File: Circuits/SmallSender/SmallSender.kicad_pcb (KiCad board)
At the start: 2 copper layers, 28 x 49.6 mm, 13 parts, among them P1 WRITER-VCC, SW1 JB-15FBP2, SW2 MKA-10110, U1 TWE_LITE_SMD, U2 HN2S01FU

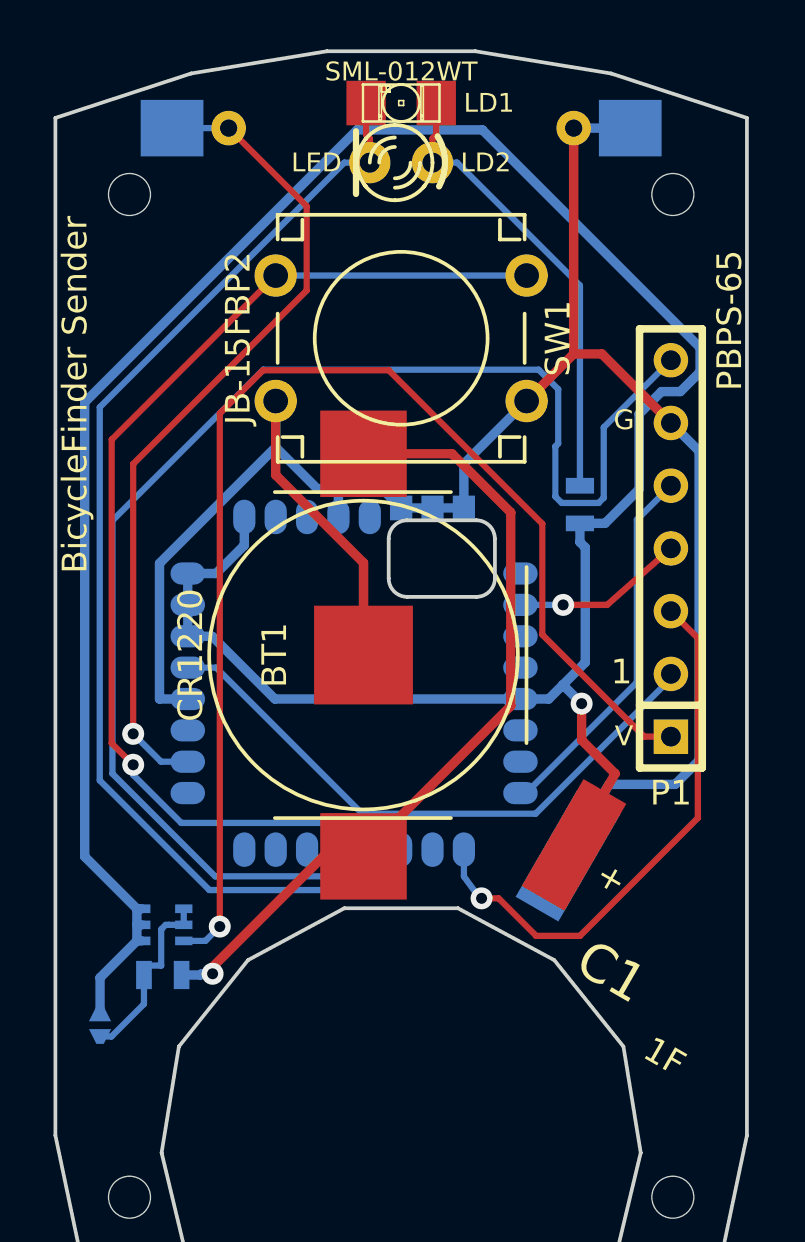
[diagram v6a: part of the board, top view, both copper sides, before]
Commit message: Added voltage monitor.
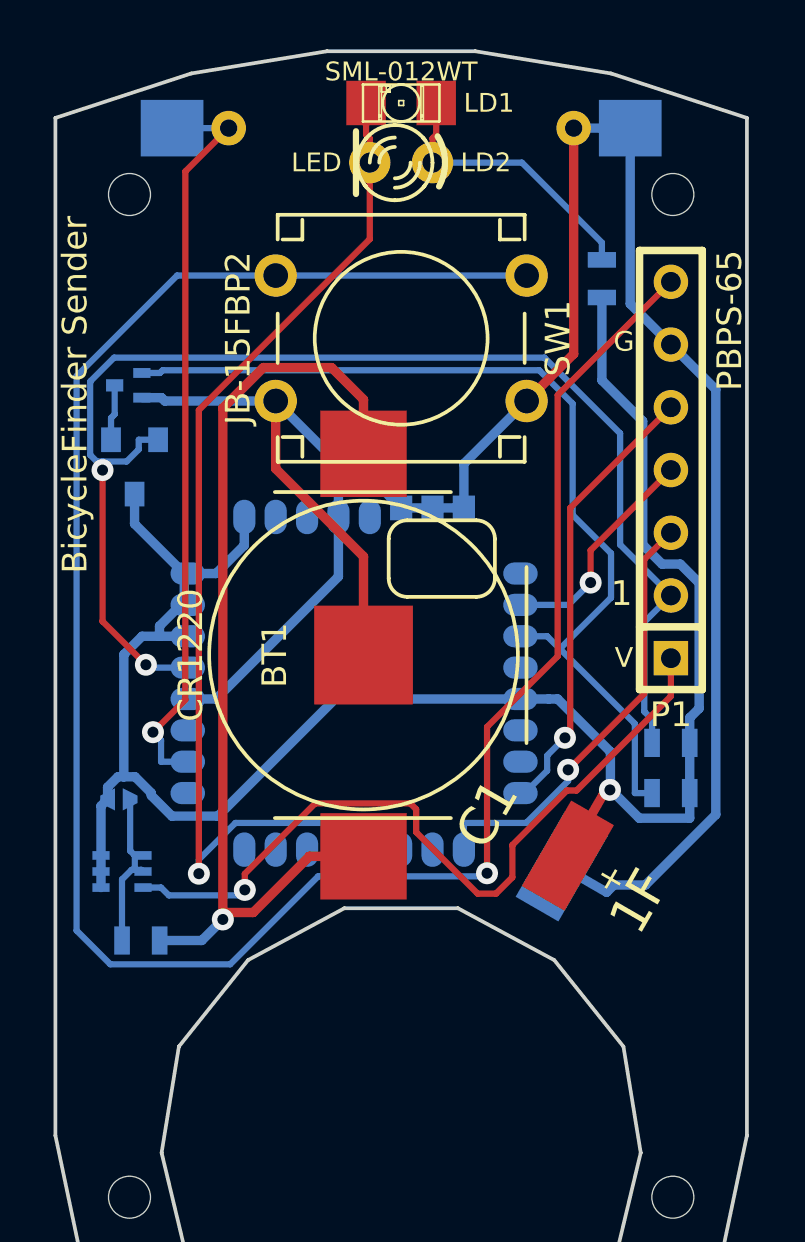
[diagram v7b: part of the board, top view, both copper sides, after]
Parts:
- added Q1: RUE002N02, EMT3, B.Cu at (15.4, 27.2)
- added R3: 10M, SM0603_Resistor, B.Cu at (37.3, 43.7)
- added R4: 10M, SM0603_Resistor, B.Cu at (37.3, 41.7)
- added U3: TCM809RVNB, SOT23, B.Cu at (15.6, 30.5)
- R1, R2: footprint SM0603 -> SM0603_Resistor
- U1: footprint TWE-001L-NC7 -> TWE-001L-SMD-noNTH
- moved R2 9.19 mm to (34.5, 22.9)
- moved JP1 9.18 mm to (15.0, 43.9), turned to 180 degrees
- moved P1 3.17 mm to (37.3, 30.6)
- moved U2 2.72 mm to (15.1, 46.9)
- moved R1 1.66 mm to (15.9, 49.7)
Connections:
- JP1 pad 1: /Vcc -> /CHG
- JP1 pad 2: /CHG -> /Vcc
- U1 pad 3: (no net) -> /DO1
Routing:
- net /DO1: track 0.00 -> 39.1 mm
- net /RST: track 24.5 -> 54.2 mm, vias 0 -> 2
- net /Vcc: track 107.9 -> 79.2 mm
- net /CFG: track 57.6 -> 32.9 mm, vias 0 -> 1
- net /3V3: track 50.2 -> 31.1 mm
- net GND: track 82.8 -> 95.5 mm
- net /DI1: track 43.7 -> 56.1 mm, vias 1 -> 0
- net /LED: track 18.6 -> 11.4 mm
- net /3V: track 32.9 -> 39.4 mm
- net /RXD: track 22.1 -> 17.8 mm
- net /DO4: track 48.0 -> 44.6 mm, vias 0 -> 1
- net /DI4: track 33.7 -> 30.4 mm
- net /TXD: track 15.1 -> 18.2 mm, vias 0 -> 1
- net /QGND: track 0.00 -> 2.26 mm
- net /PRG: track 6.96 -> 9.12 mm
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
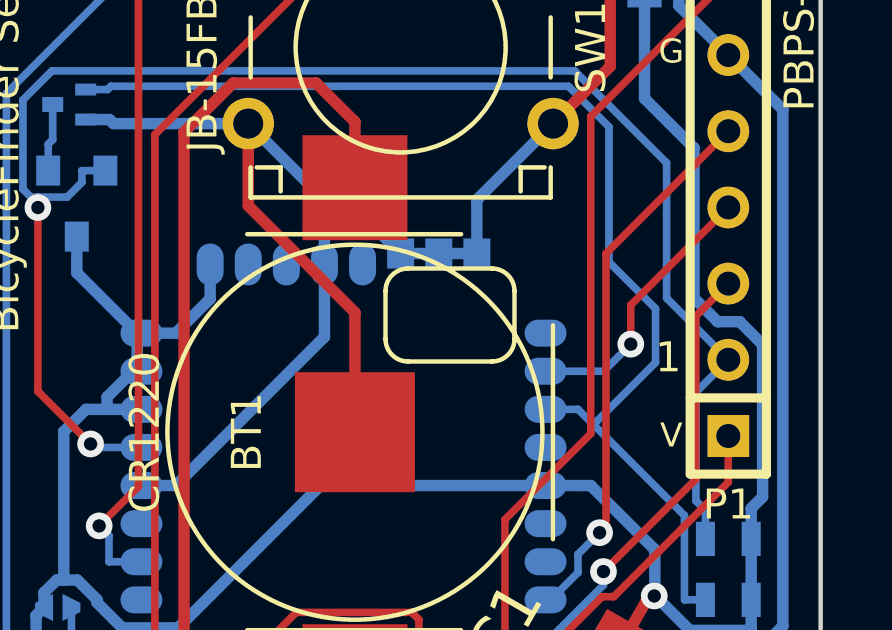
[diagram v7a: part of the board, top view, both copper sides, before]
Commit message: Replaced TWE-Lite module.
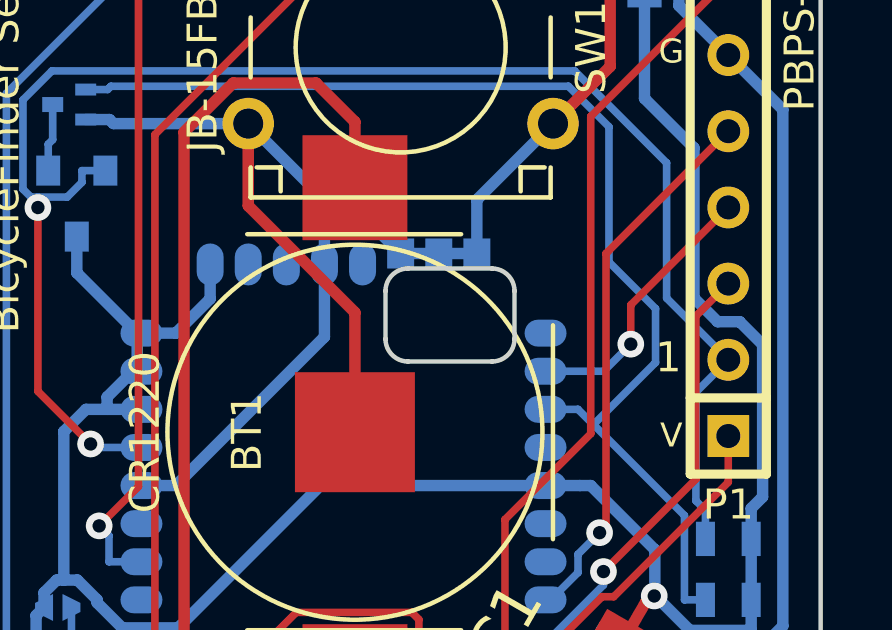
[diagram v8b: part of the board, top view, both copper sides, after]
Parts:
- U1: footprint TWE-001L-SMD-noNTH -> TWE-001L-NC7
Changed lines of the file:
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@@
     (links 49)
     (no_connects 0)
-    (area 11.259889 13.321999 40.745001 68.780001)
+    (area 12.086999 13.321999 40.745001 68.780001)
     (thickness 1)
     (drawings 0)
@@
     )
   )
-  (module TWE-001L-SMD-noNTH (layer B.Cu)
+  (module SE-5R5-D105VYV   placed (layer F.Cu)
+    (at 26.416 57.912 60)
+    (descr "Capacitor, EDLC, cyl 18.5x4mm")
+    (fp_text reference C1 (at 13.335 -3.683 60) (layer F.SilkS)
+      (effects (font (size 1.524 1.524) (thickness 0.3048)))
+    )
+    (fp_text value 1F (at 13.335 3.429 60) (layer F.SilkS)
+      (effects (font (size 1.524 1.524) (thickness 0.3048)))
+    )
+    (fp_text user + (at 13.55 1.95 60) (layer F.SilkS)
+      (effects (font (size 1 1) (thickness 0.15)))
+    )
+    (fp_circle (center 0 0) (end 9.5 0) (layer Cmts.User) (width 0.15))
+    (pad 1 smd rect (at 13.5 0 60) (size 4 2)
+      (layers F.Cu F.Paste F.Mask)
+      (net 15 /Vcc)
+    )
+    (pad 2 smd rect (at 13 0 60) (size 4 2)
+      (layers B.Cu B.Paste B.Mask)
+      (net 16 GND)
+    )
+    (model ../packages3d/SE-5R5-D105VYV.wrl
+      (at (xyz 0 0 -0.03937007874))
+      (scale (xyz 0.393701 0.393701 0.393701))
+      (rotate (xyz 0 0 0))
+    )
+  )
+  (module EMT3 (layer B.Cu)
+    (at 15.367 27.178 270)
+    (descr EMT3)
+    (attr smd)
+    (fp_text reference Q1 (at 0 -1.651 270) (layer B.SilkS)
+      (effects (font (size 0.29972 0.29972) (thickness 0.06096)) (justify mirror))
+    )
+    (fp_text value RUE002N02 (at 0 -0.3302 270) (layer B.SilkS) hide
+      (effects (font (size 0.29972 0.29972) (thickness 0.06096)) (justify mirror))
+    )
+    (fp_line (start -0.8 0.4) (end 0.8 0.4) (layer B.SilkS) (width 0.127))
+    (fp_line (start 0.8 0.4) (end 0.8 -0.4) (layer B.SilkS) (width 0.127))
+    (fp_line (start 0.8 -0.4) (end -0.8 -0.4) (layer B.SilkS) (width 0.127))
+    (fp_line (start -0.8 -0.4) (end -0.8 0.4) (layer B.SilkS) (width 0.127))
+    (pad G smd rect (at -0.5 -0.55 270) (size 0.4 0.7)
+      (layers B.Cu B.Paste B.Mask)
+      (net 7 /DO1)
+    )
+    (pad S smd rect (at 0.5 -0.55 270) (size 0.4 0.7)
+      (layers B.Cu B.Paste B.Mask)
+      (net 16 GND)
+    )
+    (pad D smd rect (at 0 0.55 270) (size 0.5 0.7)
+      (layers B.Cu B.Paste B.Mask)
+      (net 11 /QGND)
+    )
+    (model ../../../kicad-lib/packages3d/EMT3.wrl
+      (at (xyz 0 0 0))
+      (scale (xyz 0.3937007874 0.3937007874 0.3937007874))
+      (rotate (xyz 0 0 0))
+    )
+  )
+  (module TWE-001L-NC7 (layer B.Cu)
     (at 24.511 39.243 180)
     (fp_text reference U1 (at 0.1 9.35 180) (layer B.SilkS)
@@
       (effects (font (size 1 1) (thickness 0.15)) (justify mirror))
     )
-    (fp_arc (start -4.95 4.25) (end -4.95 3.5) (angle -90) (layer F.SilkS) (width 0.15))
-    (fp_line (start -5.7 4.25) (end -5.7 5.85) (layer F.SilkS) (width 0.15))
-    (fp_arc (start -4.95 5.85) (end -5.7 5.85) (angle -90) (layer F.SilkS) (width 0.15))
-    (fp_line (start -2.15 6.6) (end -4.95 6.6) (layer F.SilkS) (width 0.15))
-    (fp_arc (start -2.15 5.85) (end -2.15 6.6) (angle -90) (layer F.SilkS) (width 0.15))
-    (fp_line (start -1.4 5.85) (end -1.4 4.25) (layer F.SilkS) (width 0.15))
-    (fp_arc (start -2.15 4.25) (end -1.4 4.25) (angle -90) (layer F.SilkS) (width 0.15))
-    (fp_line (start -2.15 3.5) (end -4.95 3.5) (layer F.SilkS) (width 0.15))
+    (fp_arc (start -4.95 4.25) (end -4.95 3.5) (angle -90) (layer Edge.Cuts) (width 0.15))
+    (fp_line (start -5.7 4.25) (end -5.7 5.85) (layer Edge.Cuts) (width 0.15))
+    (fp_arc (start -4.95 5.85) (end -5.7 5.85) (angle -90) (layer Edge.Cuts) (width 0.15))
+    (fp_line (start -2.15 6.6) (end -4.95 6.6) (layer Edge.Cuts) (width 0.15))
+    (fp_arc (start -2.15 5.85) (end -2.15 6.6) (angle -90) (layer Edge.Cuts) (width 0.15))
+    (fp_line (start -1.4 5.85) (end -1.4 4.25) (layer Edge.Cuts) (width 0.15))
+    (fp_arc (start -2.15 4.25) (end -1.4 4.25) (angle -90) (layer Edge.Cuts) (width 0.15))
+    (fp_line (start -2.15 3.5) (end -4.95 3.5) (layer Edge.Cuts) (width 0.15))
     (fp_line (start -6.985 6.985) (end -6.985 -6.985) (layer B.SilkS) (width 0.15))
     (fp_line (start -6.985 -6.985) (end 6.985 -6.985) (layer B.SilkS) (width 0.15))
     (fp_line (start 6.985 -6.985) (end 6.985 6.985) (layer B.SilkS) (width 0.15))
     (fp_line (start 6.985 6.985) (end -6.985 6.985) (layer B.SilkS) (width 0.15))
-    (fp_line (start -4.3 8) (end -4.3 13.7) (layer B.SilkS) (width 0.15))
-    (fp_line (start -4.3 13.7) (end 5.7 13.7) (layer B.SilkS) (width 0.15))
-    (fp_line (start 5.7 13.7) (end 5.7 19.7) (layer B.SilkS) (width 0.15))
-    (fp_line (start 5.7 19.7) (end -4.3 19.7) (layer B.SilkS) (width 0.15))
+    (fp_line (start -4.3 8) (end -4.3 13.7) (layer Cmts.User) (width 0.15))
+    (fp_line (start -4.3 13.7) (end 5.7 13.7) (layer Cmts.User) (width 0.15))
+    (fp_line (start 5.7 13.7) (end 5.7 19.7) (layer Cmts.User) (width 0.15))
+    (fp_line (start 5.7 19.7) (end -4.3 19.7) (layer Cmts.User) (width 0.15))
     (pad 1 smd oval (at -6.735 4.445 90) (size 0.9 1.4)
       (layers B.Cu B.Paste B.Mask)
@@
       (rotate (xyz 0 0 0))
     )
-  )
-  (module SE-5R5-D105VYV   placed (layer F.Cu)
-    (at 26.416 57.912 60)
-    (descr "Capacitor, EDLC, cyl 18.5x4mm")
-    (fp_text reference C1 (at 13.335 -3.683 60) (layer F.SilkS)
-      (effects (font (size 1.524 1.524) (thickness 0.3048)))
-    )
-    (fp_text value 1F (at 13.335 3.429 60) (layer F.SilkS)
-      (effects (font (size 1.524 1.524) (thickness 0.3048)))
-    )
-    (fp_text user + (at 13.55 1.95 60) (layer F.SilkS)
-      (effects (font (size 1 1) (thickness 0.15)))
-    )
-    (fp_circle (center 0 0) (end 9.5 0) (layer Cmts.User) (width 0.15))
-    (pad 1 smd rect (at 13.5 0 60) (size 4 2)
-      (layers F.Cu F.Paste F.Mask)
-      (net 15 /Vcc)
-    )
-    (pad 2 smd rect (at 13 0 60) (size 4 2)
-      (layers B.Cu B.Paste B.Mask)
-      (net 16 GND)
-    )
-    (model ../packages3d/SE-5R5-D105VYV.wrl
-      (at (xyz 0 0 -0.03937007874))
-      (scale (xyz 0.393701 0.393701 0.393701))
-      (rotate (xyz 0 0 0))
-    )
-  )
-  (module EMT3 (layer B.Cu)
-    (at 15.367 27.178 270)
-    (descr EMT3)
-    (attr smd)
-    (fp_text reference Q1 (at 0 -1.651 270) (layer B.SilkS)
-      (effects (font (size 0.29972 0.29972) (thickness 0.06096)) (justify mirror))
-    )
-    (fp_text value RUE002N02 (at 0 -0.3302 270) (layer B.SilkS) hide
-      (effects (font (size 0.29972 0.29972) (thickness 0.06096)) (justify mirror))
-    )
-    (fp_line (start -0.8 0.4) (end 0.8 0.4) (layer B.SilkS) (width 0.127))
-    (fp_line (start 0.8 0.4) (end 0.8 -0.4) (layer B.SilkS) (width 0.127))
-    (fp_line (start 0.8 -0.4) (end -0.8 -0.4) (layer B.SilkS) (width 0.127))
-    (fp_line (start -0.8 -0.4) (end -0.8 0.4) (layer B.SilkS) (width 0.127))
-    (pad G smd rect (at -0.5 -0.55 270) (size 0.4 0.7)
-      (layers B.Cu B.Paste B.Mask)
-      (net 7 /DO1)
-    )
-    (pad S smd rect (at 0.5 -0.55 270) (size 0.4 0.7)
-      (layers B.Cu B.Paste B.Mask)
-      (net 16 GND)
-    )
-    (pad D smd rect (at 0 0.55 270) (size 0.5 0.7)
-      (layers B.Cu B.Paste B.Mask)
-      (net 11 /QGND)
-    )
-    (model ../../../kicad-lib/packages3d/EMT3.wrl
-      (at (xyz 0 0 0))
-      (scale (xyz 0.3937007874 0.3937007874 0.3937007874))
-      (rotate (xyz 0 0 0))
-    )
